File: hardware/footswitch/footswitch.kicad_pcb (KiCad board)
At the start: 2 copper layers, 34 x 58 mm, 6 parts, among them J1 Conn_02x05_Counter_Clockwise

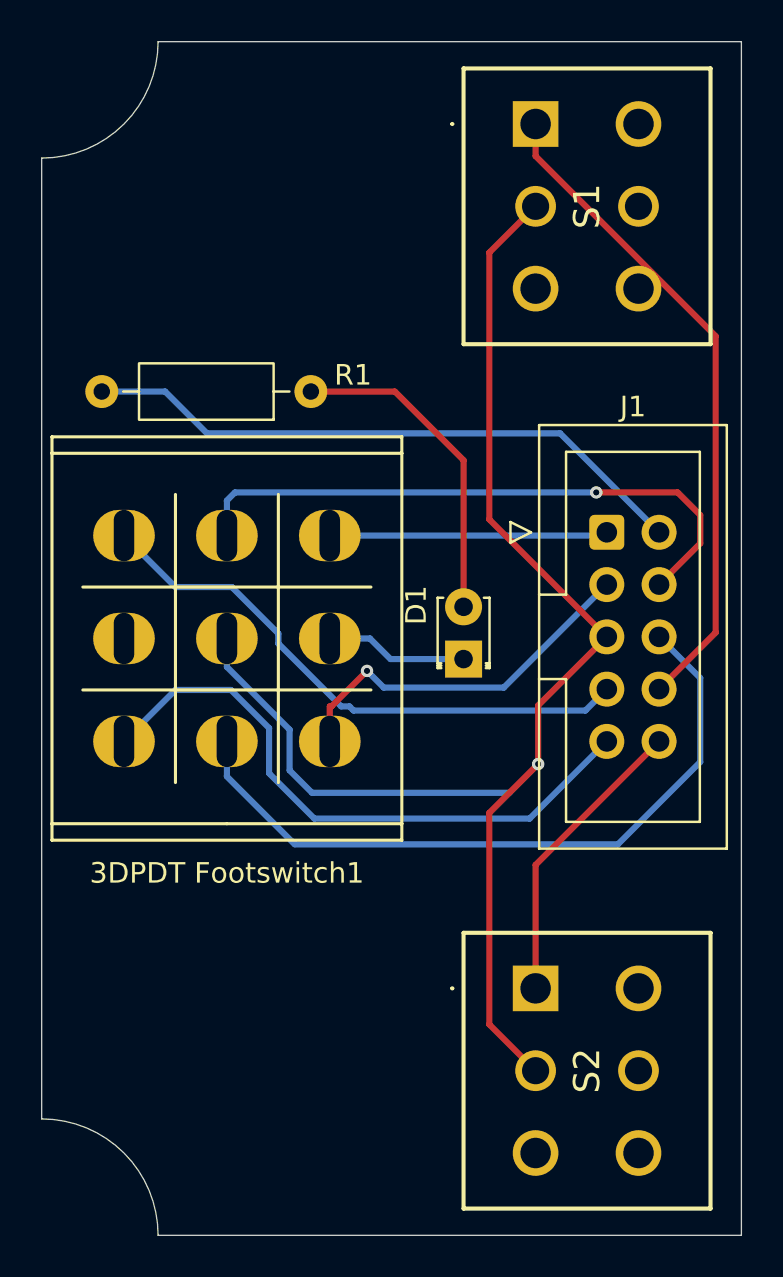
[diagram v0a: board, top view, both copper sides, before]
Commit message: Adjust footprints for Tayda compact footswitches
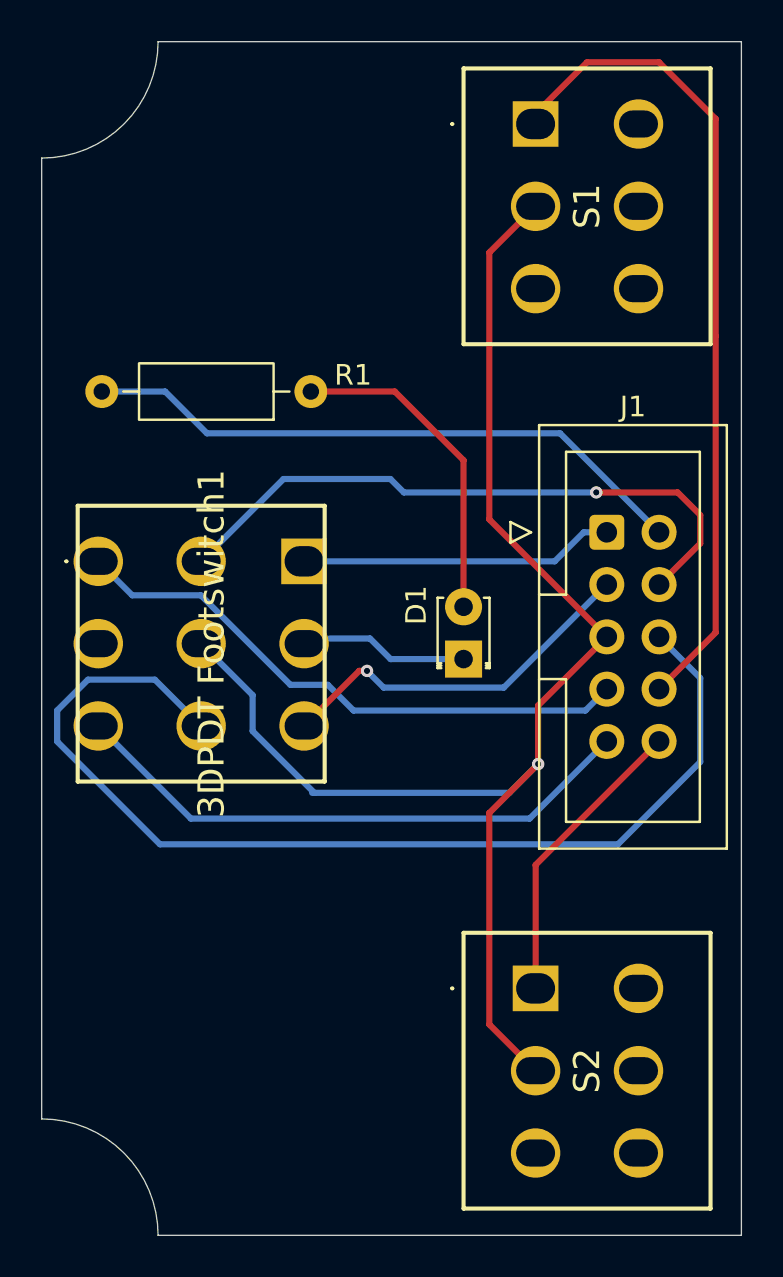
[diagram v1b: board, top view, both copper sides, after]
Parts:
- 3DPDT Footswitch1: footprint Button_Switch_THT:Switches_Stomp_Switch_3PDT -> Library:0.7 footswitches - 3dpdt tayda
- S1, S2: footprint pcb switch:DPDT momentary footswitch -> Library:0.7 footswitches
- moved 3DPDT Footswitch1 5.30 mm to (135.2, 90.2)
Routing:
- net /conn6: track 34.6 -> 51.9 mm
- net /conn8: track 32.2 -> 40.3 mm
- net /conn1: track 13.5 -> 15.5 mm
- net /conn9: track 29.9 -> 28.1 mm
- net /conn4: track 29.5 -> 30.8 mm

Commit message: Remove line in switch - TL074 is fine
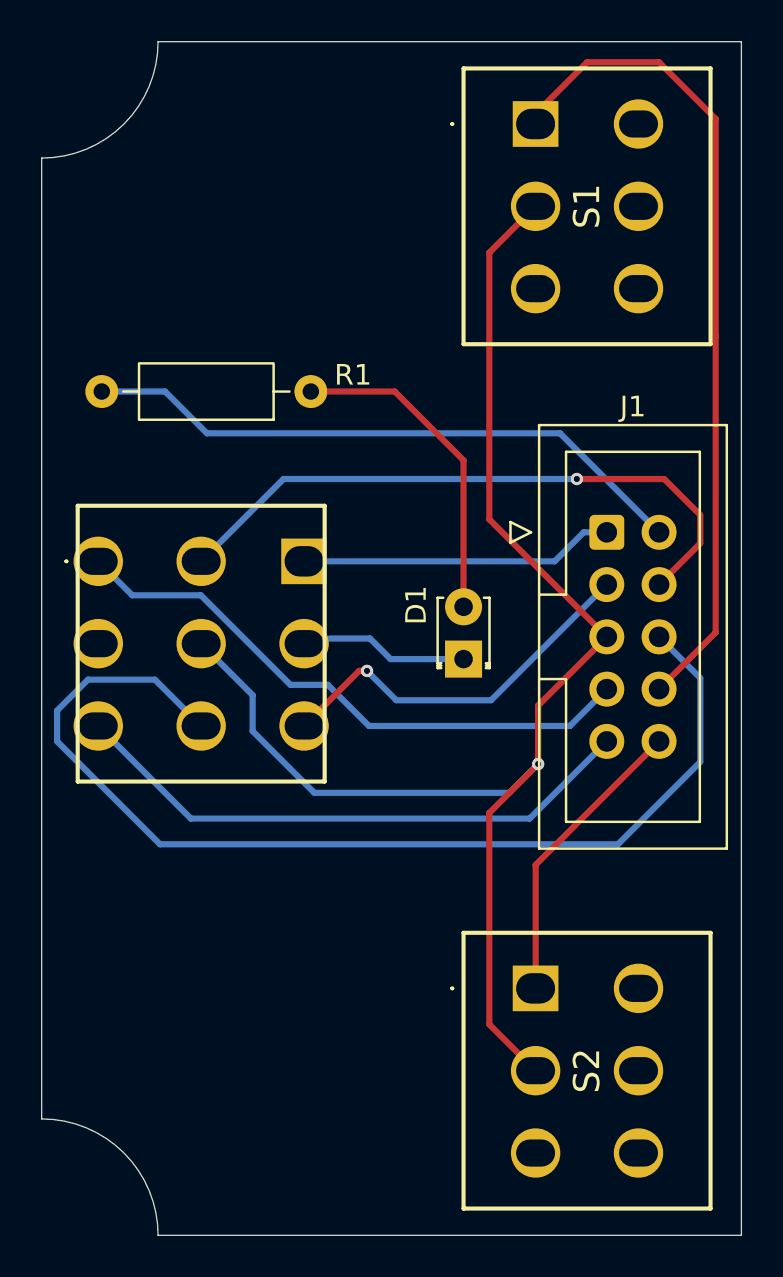
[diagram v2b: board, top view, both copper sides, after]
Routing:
- net /conn7: track 28.1 -> 28.8 mm
- net /conn3: track 18.8 -> 19.3 mm
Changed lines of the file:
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@@
 			(at 4 -3 270)
 			(layer "F.SilkS")
+			(hide yes)
 			(effects
 				(font
@@
 			)
 			(layer "F.Fab")
-		)
-		(fp_text user "${REFERENCE}"
-			(at 4 -2.5 270)
-			(layer "F.Fab")
-			(effects
-				(font
-					(size 1.27 1.27)
-					(thickness 0.254)
-				)
-			)
 		)
 		(pad "1" thru_hole rect
@@
 	)
 	(segment
+		(start 160.25 86.25)
+		(end 162 88)
+		(width 0.3)
+		(layer "F.Cu")
+		(net 3)
+	)
+	(segment
 		(start 162 89.38)
-		(end 162 88)
+		(end 160 91.38)
 		(width 0.3)
 		(layer "F.Cu")
@@
 	)
 	(segment
-		(start 160.9023 86.9023)
-		(end 156.9469 86.9023)
+		(start 162 88)
+		(end 162 89.38)
 		(width 0.3)
 		(layer "F.Cu")
@@
 	)
 	(segment
-		(start 162 88)
-		(end 160.9023 86.9023)
+		(start 156 86.25)
+		(end 160.25 86.25)
 		(width 0.3)
 		(layer "F.Cu")
 		(net 3)
 	)
-	(segment
-		(start 160 91.38)
-		(end 162 89.38)
-		(width 0.3)
-		(layer "F.Cu")
-		(net 3)
-	)
 	(via
-		(at 156.9469 86.9023)
+		(at 156 86.25)
 		(size 0.6)
 		(drill 0.3)
@@
 	)
 	(segment
-		(start 147.5977 86.9023)
-		(end 146.9454 86.25)
+		(start 156 86.25)
+		(end 141.75 86.25)
 		(width 0.3)
 		(layer "B.Cu")
@@
 	)
 	(segment
-		(start 146.9454 86.25)
-		(end 141.75 86.25)
-		(width 0.3)
-		(layer "B.Cu")
-		(net 3)
-	)
-	(segment
-		(start 156.9469 86.9023)
-		(end 147.5977 86.9023)
-		(width 0.3)
-		(layer "B.Cu")
-		(net 3)
-	)
-	(segment
 		(start 155.1899 84.0299)
 		(end 138.0299 84.0299)
@@
 	(segment
 		(start 157.46 96.46)
-		(end 156.42 97.5)
+		(end 155.67 98.25)
 		(width 0.3)
 		(layer "B.Cu")
@@
 	)
 	(segment
+		(start 145.905577 98.25)
+		(end 143.905577 96.25)
+		(width 0.3)
+		(layer "B.Cu")
+		(net 5)
+	)
+	(segment
+		(start 142.084867 96.25)
+		(end 137.735867 91.901)
+		(width 0.3)
+		(layer "B.Cu")
+		(net 5)
+	)
+	(segment
 		(start 134.401 91.901)
 		(end 132.75 90.25)
@@
 	)
 	(segment
-		(start 156.42 97.5)
-		(end 145.155577 97.5)
-		(width 0.3)
-		(layer "B.Cu")
-		(net 5)
-	)
-	(segment
-		(start 145.155577 97.5)
-		(end 143.905577 96.25)
-		(width 0.3)
-		(layer "B.Cu")
-		(net 5)
-	)
-	(segment
-		(start 142.084867 96.25)
-		(end 137.735867 91.901)
+		(start 155.67 98.25)
+		(end 145.905577 98.25)
 		(width 0.3)
 		(layer "B.Cu")
@@
 	)
 	(segment
-		(start 152.455 96.385)
-		(end 146.6197 96.385)
+		(start 147.2347 97)
+		(end 145.8082 95.5735)
 		(width 0.3)
 		(layer "B.Cu")
@@
 	)
 	(segment
-		(start 146.6197 96.385)
-		(end 145.8082 95.5735)
+		(start 157.46 91.38)
+		(end 151.84 97)
 		(width 0.3)
 		(layer "B.Cu")
@@
 	)
 	(segment
-		(start 157.46 91.38)
-		(end 152.455 96.385)
+		(start 151.84 97)
+		(end 147.2347 97)
 		(width 0.3)
 		(layer "B.Cu")
@@
 		(width 0.3)
 		(layer "B.Cu")
-		(net 9)
-	)
-	(segment
-		(start 143.14221 101.5)
-		(end 143.25 101.5)
-		(width 0.3)
-		(layer "B.Cu")
